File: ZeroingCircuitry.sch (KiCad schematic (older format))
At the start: 8 parts, among them U2 74HC123, U3 74HC08

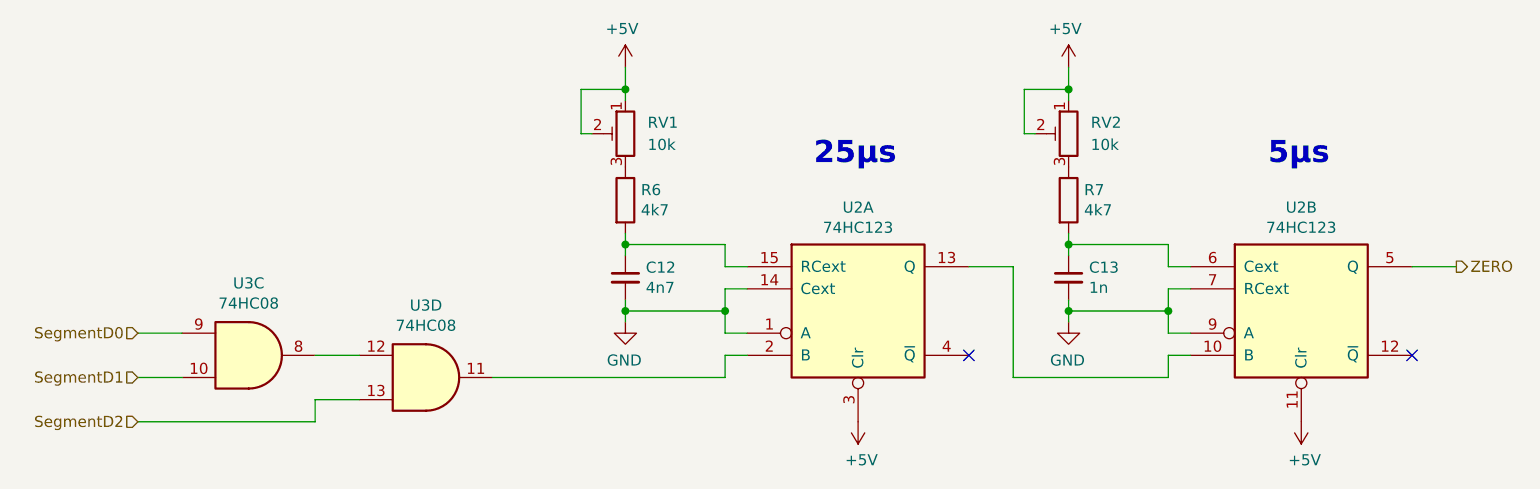
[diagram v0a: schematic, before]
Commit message: Fixed some bugs, finished block symbols
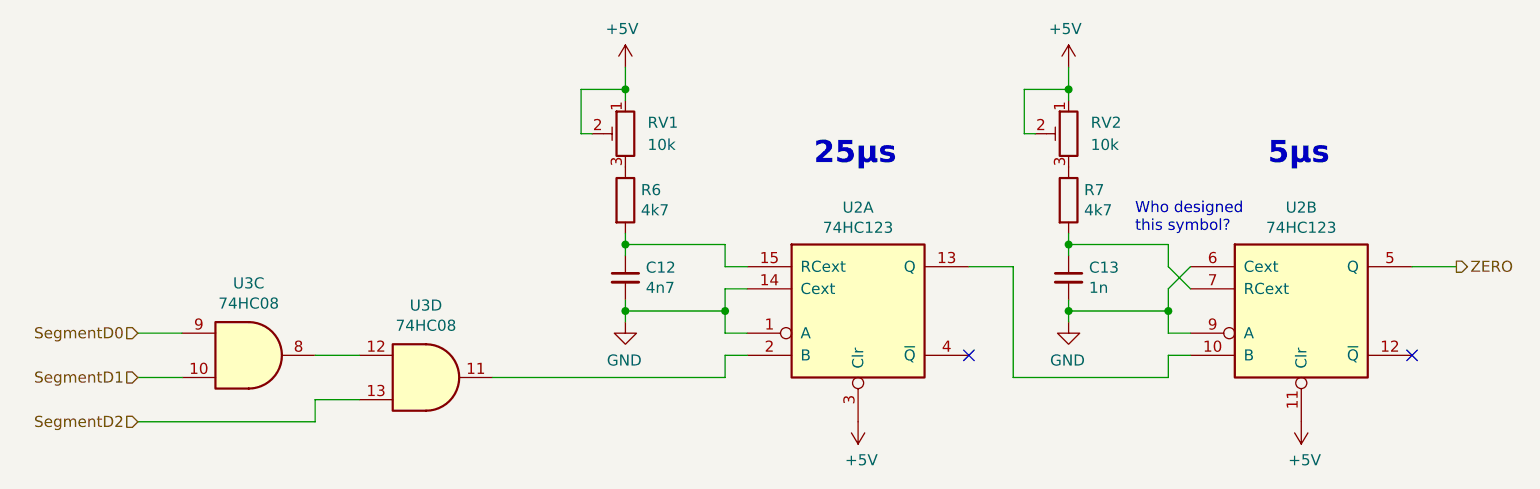
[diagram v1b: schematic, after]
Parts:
- RV1, RV2: footprint Potentiometer_THT:Potentiometer_Bourns_3299W_Vertical -> Potentiometer_THT:Potentiometer_Bourns_3296W_Vertical
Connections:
- net GND: now also U2.6 (Cext); no longer U2.7 (RCext)
- net at C13.1, R7.2: now also U2.7 (RCext); no longer U2.6 (Cext)
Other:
- note added: "Who designed\nthis symbol?"
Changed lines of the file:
@@
 encoding utf-8
 Sheet 6 13
-Title ""
-Date ""
-Rev ""
-Comp ""
+Title "Zero Signal Generator"
+Date "2021-04-20"
+Rev "2.0"
+Comp "Filip Piórski"
 Comment1 ""
 Comment2 ""
@@
 F 0 "RV1" H 4400 3050 50  0000 R CNN
 F 1 "10k" H 4400 2950 50  0000 R CNN
-F 2 "Potentiometer_THT:Potentiometer_Bourns_3299W_Vertical" H 4500 3000 50  0001 C CNN
+F 2 "Potentiometer_THT:Potentiometer_Bourns_3296W_Vertical" H 4500 3000 50  0001 C CNN
 F 3 "~" H 4500 3000 50  0001 C CNN
 	1    4500 3000
@@
 F 0 "RV2" H 6400 3050 50  0000 R CNN
 F 1 "10k" H 6400 2950 50  0000 R CNN
-F 2 "Potentiometer_THT:Potentiometer_Bourns_3299W_Vertical" H 6500 3000 50  0001 C CNN
+F 2 "Potentiometer_THT:Potentiometer_Bourns_3296W_Vertical" H 6500 3000 50  0001 C CNN
 F 3 "~" H 6500 3000 50  0001 C CNN
 	1    6500 3000
@@
 Wire Wire Line
 	6500 3750 6500 3800
-Wire Wire Line
-	6500 3800 6950 3800
-Wire Wire Line
-	6950 3800 6950 3700
-Wire Wire Line
-	6950 3700 7050 3700
 Connection ~ 6500 3800
 Wire Wire Line
 	6500 3800 6500 3850
-Wire Wire Line
-	7050 3600 6950 3600
-Wire Wire Line
-	6950 3600 6950 3500
-Wire Wire Line
-	6950 3500 6500 3500
 Connection ~ 6500 3500
 Wire Wire Line
@@
 Wire Wire Line
 	6950 3800 6950 3900
-Wire Wire Line
-	6950 3900 7050 3900
-Connection ~ 6950 3800
 Wire Wire Line
 	7050 4000 6950 4000
@@
 ZERO
 NoConn ~ 8050 4000
+Wire Wire Line
+	6500 3800 6950 3800
+Wire Wire Line
+	6950 3900 7050 3900
+Wire Wire Line
+	6950 3800 6950 3700
+Wire Wire Line
+	6950 3700 7050 3600
+Connection ~ 6950 3800
+Wire Wire Line
+	6950 3600 6950 3500
+Wire Wire Line
+	6950 3600 7050 3700
+Wire Wire Line
+	6500 3500 6950 3500
+Text Notes 6800 3450 0    50   ~ 0
+Who designed\nthis symbol?
 $EndSCHEMATC
